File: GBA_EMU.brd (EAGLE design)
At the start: 130.7 x 72.9 mm, 74 parts, among them IC1 MEGA16U2, Q1 MOSFET-PCHANNEL, SW1 LEFT, SW2 RIGHT, SW3 PWR_SWITCH, U1 RPI-ZERO, U2 FT230X, U3 MCP1642B-ADJ, U4 LM4875, U5 V_REG_LDOSMD2, U6 MIC7221, U7 AZV321, X2 HEADPHONE

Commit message: added some descriptions and moved some labels
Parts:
- added R17: 4.7k, rcl:R0805
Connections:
- net N$27 renamed COPRO_TX
- net N$29 renamed COPRO_RX
- net AVR_VCC: now also R17.2
- net RESET: now also R17.1
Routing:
- net RESET: track 36.6 -> 41.0 mm, vias 2 -> 3
- net AVR_VCC: track 65.8 -> 67.3 mm
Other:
- board text added: "GND"
- board text added: "MISO"
- board text added: "MOSI"
- board text added: "RESET"
- board text added: "RX"
- board text added: "SCK"
- board text added: "TX"
- board text added: "VCC"
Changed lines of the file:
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@@
 Taylor Lewis
 Carson Bunker</text>
+<text x="23.876" y="57.404" size="0.6096" layer="21">TX</text>
+<text x="23.876" y="56.134" size="0.6096" layer="21">RX</text>
+<text x="23.368" y="58.674" size="0.6096" layer="21">VCC</text>
+<text x="27.178" y="60.071" size="0.6096" layer="21">GND</text>
+<text x="33.528" y="28.829" size="0.6096" layer="21">MOSI</text>
+<text x="25.654" y="25.146" size="0.6096" layer="21">RESET</text>
+<text x="26.162" y="30.099" size="0.6096" layer="21">SCK</text>
+<text x="25.781" y="31.496" size="0.6096" layer="21">MISO</text>
+<text x="33.401" y="31.242" size="0.6096" layer="21">VCC</text>
 </plain>
 <attributes>
@@
 <attribute name="VALUE" x="98.179" y="84.328" size="1.27" layer="27" rot="R180"/>
 </element>
-<element name="J1" library="SparkFun-Connectors" package="1X04-1.27MM" value="" x="26.035" y="56.515" rot="R90"/>
+<element name="J1" library="SparkFun-Connectors" package="1X04-1.27MM" value="" x="26.035" y="56.515" smashed="yes" rot="R90">
+<attribute name="VALUE" x="27.686" y="56.007" size="0.4064" layer="27" rot="R90"/>
+</element>
+<element name="R17" library="rcl" package="R0805" value="4.7k" x="33.274" y="39.497" smashed="yes" rot="MR180">
+<attribute name="NAME" x="33.909" y="38.227" size="1.0668" layer="26" rot="MR180"/>
+<attribute name="VALUE" x="35.179" y="40.132" size="0.762" layer="28" rot="MR180"/>
+</element>
 </elements>
 <signals>
@@
 <via x="26.035" y="41.275" extent="1-16" drill="0.6"/>
 <wire x1="26.035" y1="41.275" x2="29.21" y2="41.275" width="0.3048" layer="1"/>
-<wire x1="29.21" y1="41.275" x2="29.21" y2="35.56" width="0.3048" layer="1"/>
+<wire x1="29.21" y1="41.275" x2="29.21" y2="37.973" width="0.3048" layer="1"/>
+<wire x1="29.21" y1="37.973" x2="29.21" y2="35.56" width="0.3048" layer="1"/>
 <wire x1="29.21" y1="35.56" x2="31.115" y2="35.56" width="0.3048" layer="1"/>
 <wire x1="31.115" y1="35.56" x2="31.115" y2="34.671" width="0.3048" layer="1"/>
@@
 <wire x1="33.655" y1="27.94" x2="29.21" y2="27.94" width="0.3048" layer="16"/>
 <wire x1="29.21" y1="27.94" x2="29.21" y2="26.67" width="0.3048" layer="16"/>
+<contactref element="R17" pad="1"/>
+<wire x1="32.324" y1="39.497" x2="32.324" y2="38.42" width="0.3048" layer="16"/>
+<wire x1="32.324" y1="38.42" x2="31.877" y2="37.973" width="0.3048" layer="16"/>
+<via x="31.877" y="37.973" extent="1-16" drill="0.6"/>
+<wire x1="31.877" y1="37.973" x2="29.21" y2="37.973" width="0.3048" layer="1"/>
 </signal>
 <signal name="AVR_VCC">
@@
 <via x="30.226" y="59.563" extent="1-16" drill="0.6"/>
 <wire x1="30.226" y1="59.563" x2="31.115" y2="60.325" width="0.3048" layer="16"/>
+<contactref element="R17" pad="2"/>
+<wire x1="34.224" y1="39.497" x2="35.052" y2="39.497" width="0.4064" layer="16"/>
+<wire x1="35.052" y1="39.497" x2="35.56" y2="40.005" width="0.4064" layer="16"/>
 </signal>
 <signal name="COPRO_MOSI">
@@
 <wire x1="94.869" y1="78.359" x2="94.869" y2="73.914" width="0.3048" layer="1"/>
 </signal>
-<signal name="N$27">
+<signal name="COPRO_TX">
 <contactref element="IC1" pad="9"/>
 <contactref element="J1" pad="2"/>
@@
 <wire x1="28.575" y1="57.785" x2="26.035" y2="57.785" width="0.3048" layer="1"/>
 </signal>
-<signal name="N$29">
+<signal name="COPRO_RX">
 <contactref element="IC1" pad="8"/>
 <contactref element="J1" pad="1"/>

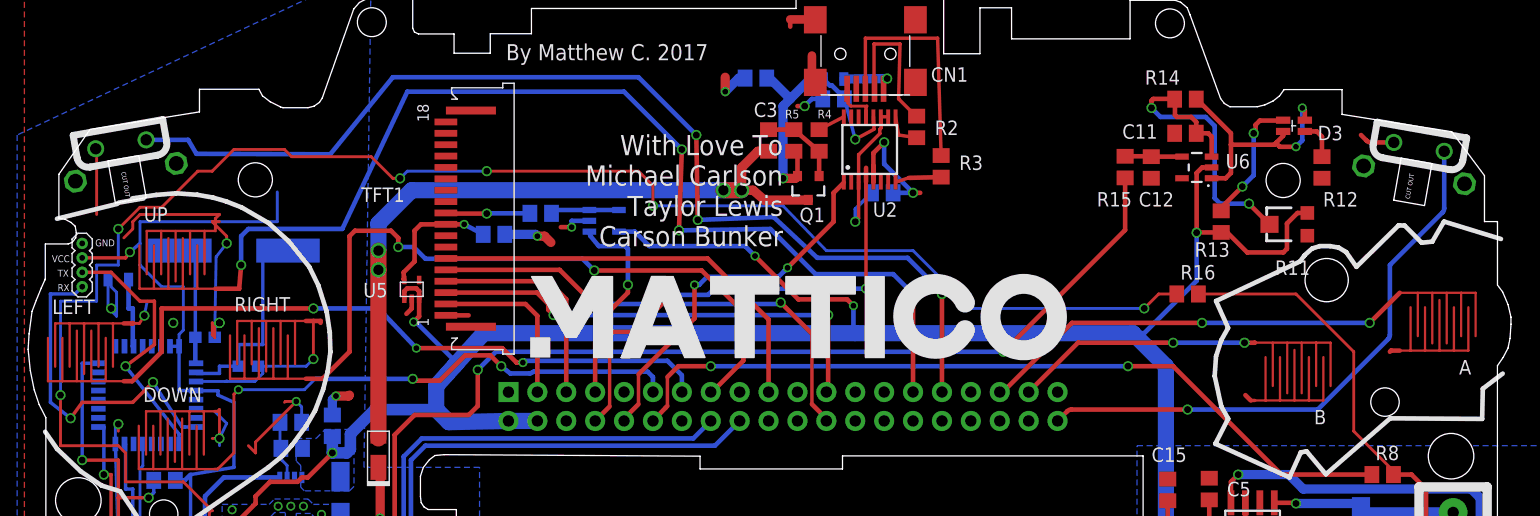
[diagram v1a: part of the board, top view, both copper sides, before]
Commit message: added L2 and R2
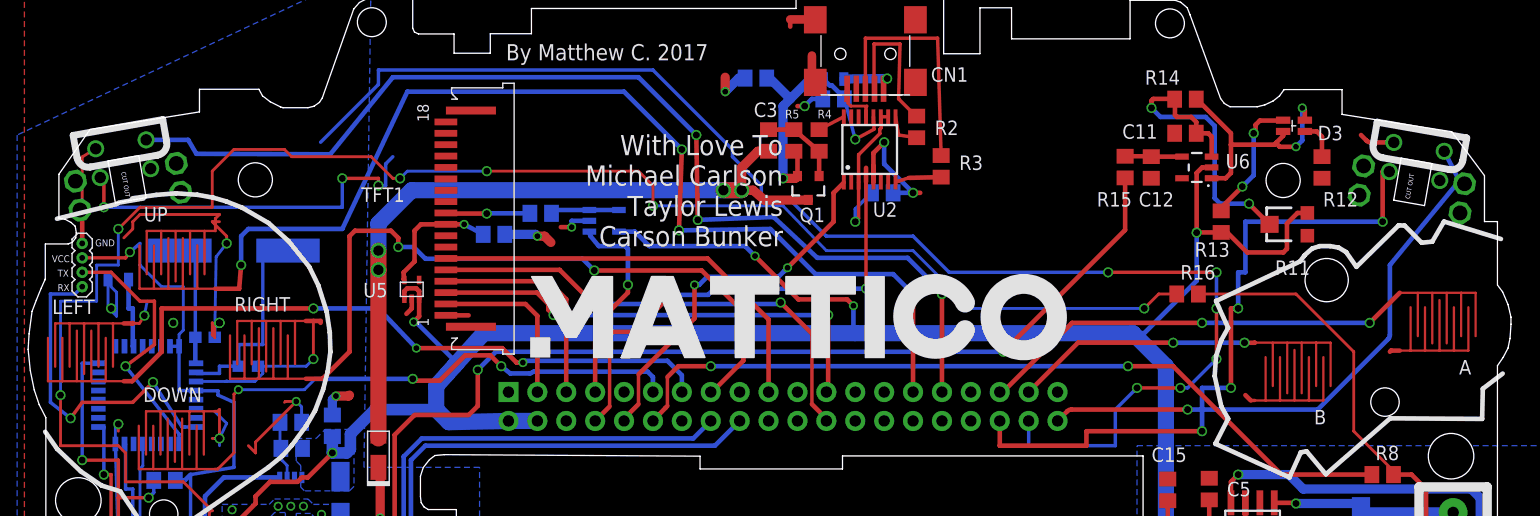
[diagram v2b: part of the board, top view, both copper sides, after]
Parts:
- added SW4: R2, custom:BUMPER_NOHOLE
- added SW5: L2, custom:BUMPER_NOHOLE
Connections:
- removed net DAC_REF: U$5.3
- new net L2_BUMP: SW5.2, U1.38
- new net R2_BUMP: SW4.2, U1.36
- net 3.3V: now also U$5.3
- net GND: now also SW4.1, SW5.1
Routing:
- net L2_BUMP: track 0.00 -> 155.6 mm, vias 0 -> 9
- net R2_BUMP: track 0.00 -> 60.5 mm, vias 0 -> 4
- net AVR_VCC: track 67.3 -> 50.7 mm
- net GND: track 146.2 -> 149.4 mm
- net DAC_OUT: track 160.9 -> 162.8 mm
- net RIGHT_BUMP: track 50.5 -> 51.0 mm
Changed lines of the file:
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@@
 <attribute name="VALUE" x="35.179" y="40.132" size="0.762" layer="28" rot="MR180"/>
 </element>
+<element name="SW4" library="custom" package="BUMPER_NOHOLE" value="R2" x="142.875" y="64.77" rot="MR10"/>
+<element name="SW5" library="custom" package="BUMPER_NOHOLE" value="L2" x="30.099" y="65.024" rot="MR350"/>
 </elements>
 <signals>
@@
 <wire x1="37.737625" y1="62.502625" x2="38.1" y2="62.865" width="0.254" layer="1"/>
 <wire x1="38.1" y1="62.865" x2="31.115" y2="62.865" width="0.254" layer="1"/>
-<wire x1="27.305" y1="62.865" x2="27.305" y2="68.56116875" width="0.254" layer="1"/>
-<wire x1="27.305" y1="68.56116875" x2="27.221940625" y2="68.644228125" width="0.254" layer="1"/>
+<wire x1="26.035" y1="62.23" x2="26.035" y2="67.92616875" width="0.254" layer="1"/>
+<wire x1="26.035" y1="67.92616875" x2="27.221940625" y2="68.644228125" width="0.254" layer="1"/>
 <wire x1="37.677790625" y1="52.067790625" x2="37.68" y2="52.07" width="0.254" layer="1"/>
 <wire x1="28.31" y1="57.15" x2="28.31" y2="54.675859375" width="0.254" layer="16"/>
@@
 <wire x1="88.265" y1="80.01" x2="88.265" y2="79.375" width="0.4064" layer="1"/>
 <wire x1="90.17" y1="74.93" x2="90.17" y2="76.835" width="0.762" layer="1"/>
+<contactref element="SW4" pad="1"/>
+<contactref element="SW5" pad="1"/>
+<wire x1="26.035" y1="62.23" x2="26.035" y2="60.325" width="0.4064" layer="1"/>
 <wire x1="40.64" y1="42.545" x2="38.1" y2="42.545" width="0" layer="19" extent="1-16"/>
+<wire x1="96.52" y1="69.215" x2="94.925" y2="71.455" width="0" layer="19" extent="1-16"/>
 <wire x1="31.75" y1="26.67" x2="39.21125" y2="34.66125" width="0" layer="19" extent="16-16"/>
 </signal>
@@
 <signal name="3.3V">
 <contactref element="U1" pad="1"/>
+<contactref element="U$5" pad="3"/>
+<wire x1="33.95" y1="22.86" x2="63.5" y2="47.26" width="0" layer="19" extent="1-1"/>
 </signal>
 <signal name="2.8V">
@@
 <contactref element="SW2" pad="2"/>
 <contactref element="U1" pad="40"/>
-<wire x1="145.743790625" y1="68.41905" x2="145.743790625" y2="63.4042125" width="0.4064" layer="16"/>
-<wire x1="145.743790625" y1="63.4042125" x2="145.595" y2="63.045" width="0.4064" layer="16" curve="-45.000249"/>
-<wire x1="145.595" y1="63.045" x2="140.97" y2="58.42" width="0.4064" layer="16"/>
+<wire x1="145.743790625" y1="68.41905" x2="147.013790625" y2="65.9442125" width="0.4064" layer="16"/>
+<wire x1="147.013790625" y1="65.9442125" x2="146.865" y2="65.585" width="0.4064" layer="16" curve="-45.000249"/>
+<wire x1="146.865" y1="65.585" x2="140.97" y2="58.42" width="0.4064" layer="16"/>
 <wire x1="140.97" y1="58.42" x2="140.97" y2="52.280421875" width="0.4064" layer="16"/>
 <wire x1="140.97" y1="52.280421875" x2="140.821209375" y2="51.921209375" width="0.4064" layer="16" curve="-45.000249"/>
@@
 <wire x1="43.815" y1="68.58" x2="39.37" y2="68.58" width="0.254" layer="1"/>
 <wire x1="39.37" y1="68.58" x2="37.465" y2="66.675" width="0.254" layer="1"/>
-<wire x1="37.465" y1="66.675" x2="36.195" y2="66.675" width="0.254" layer="1"/>
-<wire x1="36.195" y1="66.675" x2="33.02" y2="63.5" width="0.254" layer="1"/>
-<wire x1="33.02" y1="63.5" x2="31.115" y2="63.5" width="0.254" layer="1"/>
+<wire x1="37.465" y1="66.675" x2="37.465" y2="63.5" width="0.254" layer="1"/>
+<wire x1="37.465" y1="63.5" x2="31.115" y2="63.5" width="0.254" layer="1"/>
 <wire x1="31.115" y1="63.5" x2="29.21" y2="61.595" width="0.254" layer="1"/>
 <via x="29.21" y="61.595" extent="1-16" drill="0.6"/>
@@
 <wire x1="33.02" y1="56.515" x2="31.115" y2="58.42" width="0.254" layer="16"/>
 <wire x1="31.115" y1="58.42" x2="31.115" y2="60.325" width="0.254" layer="16"/>
-<wire x1="31.115" y1="60.325" x2="31.115" y2="62.23" width="0.254" layer="16"/>
-<wire x1="31.115" y1="62.23" x2="43.18" y2="62.23" width="0.254" layer="16"/>
-<wire x1="43.18" y1="62.23" x2="43.18" y2="64.85" width="0.254" layer="16"/>
 <contactref element="J1" pad="3"/>
 <wire x1="26.035" y1="59.055" x2="29.845" y2="59.055" width="0.3048" layer="1"/>
@@
 <wire x1="31.369" y1="42.6784" x2="31.35" y2="42.6974" width="0.254" layer="16"/>
 </signal>
-<signal name="DAC_REF">
-<contactref element="U$5" pad="3"/>
-</signal>
 <signal name="N$4">
 <contactref element="R2" pad="2"/>
@@
 <wire x1="25.4" y1="55.88" x2="26.035" y2="56.515" width="0.3048" layer="16"/>
 </signal>
+<signal name="R2_BUMP">
+<contactref element="SW4" pad="2"/>
+<contactref element="U1" pad="36"/>
+<wire x1="140.91965625" y1="66.63791875" x2="140.335" y2="66.63791875" width="0.4064" layer="1"/>
+<wire x1="140.335" y1="66.63791875" x2="140.335" y2="62.23" width="0.4064" layer="1"/>
+<via x="140.335" y="62.23" extent="1-16" drill="0.6"/>
+<wire x1="140.335" y1="62.23" x2="128.27" y2="62.23" width="0.4064" layer="16"/>
+<wire x1="128.27" y1="62.23" x2="128.27" y2="57.785" width="0.4064" layer="16"/>
+<wire x1="128.27" y1="57.785" x2="127.635" y2="57.785" width="0.4064" layer="16"/>
+<wire x1="127.635" y1="57.785" x2="127.635" y2="54.61" width="0.4064" layer="16"/>
+<via x="127.635" y="54.61" extent="1-16" drill="0.6"/>
+<wire x1="127.635" y1="54.61" x2="127" y2="54.61" width="0.4064" layer="1"/>
+<wire x1="127" y1="54.61" x2="127" y2="47.625" width="0.4064" layer="1"/>
+<via x="127" y="47.625" extent="1-16" drill="0.6"/>
+<wire x1="127" y1="47.625" x2="124.46" y2="47.625" width="0.4064" layer="16"/>
+<wire x1="124.46" y1="47.625" x2="124.46" y2="43.815" width="0.4064" layer="16"/>
+<via x="124.46" y="43.815" extent="1-16" drill="0.6"/>
+<wire x1="124.46" y1="43.815" x2="114.3" y2="43.815" width="0.4064" layer="1"/>
+<wire x1="114.3" y1="43.815" x2="114.3" y2="42.545" width="0.4064" layer="1"/>
+<wire x1="114.3" y1="42.545" x2="106.68" y2="42.545" width="0.4064" layer="1"/>
+<wire x1="106.68" y1="42.545" x2="106.68" y2="44.72" width="0.4064" layer="1"/>
+</signal>
+<signal name="L2_BUMP">
+<contactref element="SW5" pad="2"/>
+<contactref element="U1" pad="38"/>
+<wire x1="27.6227125" y1="66.110503125" x2="27.94" y2="66.110503125" width="0.3048" layer="1"/>
+<wire x1="27.94" y1="66.110503125" x2="27.94" y2="63.5" width="0.3048" layer="1"/>
+<via x="27.94" y="63.5" extent="1-16" drill="0.6" shape="square"/>
+<wire x1="27.94" y1="63.5" x2="48.895" y2="63.5" width="0.3048" layer="16"/>
+<wire x1="48.895" y1="63.5" x2="48.895" y2="66.04" width="0.3048" layer="16"/>
+<via x="48.895" y="66.04" extent="1-16" drill="0.6" shape="square"/>
+<wire x1="48.895" y1="66.04" x2="52.07" y2="66.04" width="0.3048" layer="1"/>
+<wire x1="52.07" y1="66.04" x2="52.07" y2="65.405" width="0.3048" layer="1"/>
+<via x="52.07" y="65.405" extent="1-16" drill="0.6" shape="square"/>
+<wire x1="52.07" y1="65.405" x2="52.705" y2="65.405" width="0.3048" layer="16"/>
+<wire x1="52.705" y1="65.405" x2="52.705" y2="67.31" width="0.3048" layer="16"/>
+<wire x1="52.705" y1="67.31" x2="53.34" y2="67.945" width="0.3048" layer="16"/>
+<wire x1="109.22" y1="44.72" x2="109.22" y2="42.545" width="0.3048" layer="16"/>
+<wire x1="109.22" y1="42.545" x2="116.84" y2="42.545" width="0.3048" layer="16"/>
+<wire x1="116.84" y1="42.545" x2="116.84" y2="45.72" width="0.3048" layer="16"/>
+<wire x1="116.84" y1="45.72" x2="118.745" y2="47.625" width="0.3048" layer="16"/>
+<via x="118.745" y="47.625" extent="1-16" drill="0.6" shape="square"/>
+<wire x1="118.745" y1="47.625" x2="122.555" y2="47.625" width="0.3048" layer="1"/>
+<via x="122.555" y="47.625" extent="1-16" drill="0.6" shape="square"/>
+<wire x1="122.555" y1="47.625" x2="123.19" y2="47.625" width="0.3048" layer="16"/>
+<wire x1="123.19" y1="47.625" x2="125.73" y2="50.165" width="0.3048" layer="16"/>
+<via x="125.73" y="50.165" extent="1-16" drill="0.6" shape="square"/>
+<wire x1="125.73" y1="50.165" x2="125.73" y2="54.61" width="0.3048" layer="1"/>
+<via x="125.73" y="54.61" extent="1-16" drill="0.6" shape="square"/>
+<wire x1="125.73" y1="54.61" x2="125.73" y2="57.785" width="0.3048" layer="16"/>
+<via x="125.73" y="57.785" extent="1-16" drill="0.6" shape="square"/>
+<wire x1="125.73" y1="57.785" x2="116.205" y2="57.785" width="0.3048" layer="1"/>
+<via x="116.205" y="57.785" extent="1-16" drill="0.6" shape="square"/>
+<wire x1="116.205" y1="57.785" x2="102.235" y2="57.785" width="0.3048" layer="16"/>
+<wire x1="102.235" y1="57.785" x2="99.06" y2="60.96" width="0.3048" layer="16"/>
+<wire x1="99.06" y1="60.96" x2="91.44" y2="60.96" width="0.3048" layer="16"/>
+<wire x1="91.44" y1="60.96" x2="88.265" y2="64.135" width="0.3048" layer="16"/>
+<wire x1="88.265" y1="64.135" x2="85.725" y2="64.135" width="0.3048" layer="16"/>
+<wire x1="85.725" y1="64.135" x2="85.725" y2="65.405" width="0.3048" layer="16"/>
+<wire x1="85.725" y1="65.405" x2="83.185" y2="67.945" width="0.3048" layer="16"/>
+<wire x1="83.185" y1="67.945" x2="83.185" y2="68.58" width="0.3048" layer="16"/>
+<wire x1="83.185" y1="68.58" x2="76.2" y2="75.565" width="0.3048" layer="16"/>
+<wire x1="76.2" y1="75.565" x2="52.07" y2="75.565" width="0.3048" layer="16"/>
+<wire x1="52.07" y1="75.565" x2="52.07" y2="74.295" width="0.3048" layer="16"/>
+<wire x1="52.07" y1="74.295" x2="46.99" y2="69.215" width="0.3048" layer="16"/>
+<wire x1="46.99" y1="69.215" x2="48.895" y2="66.04" width="0" layer="19" extent="1-16"/>
+</signal>
 </signals>

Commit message: almost done!
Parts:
- removed X2: HEADPHONE, GBA:HEADPHONE
- added J2: AUDIO-JACK2SMD, SparkFun-Connectors:AUDIO-JACK-3.5MM-SMD
- added POT1: THUMBPOT, adafruit:THUMBWHEEL
- R1: value 27k -> 150R; device GBA:VOLUME -> SparkFun-Resistors:0603-RES
- moved R1 10.4 mm to (127.6, 23.5), flipped to the top, turned to 270 degrees
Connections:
- removed net N$13: C7.-, X2.L, X2.R
- new net N$29: C7.-, J2.RING, J2.TIP, R1.2
- net 5V: now also POT1.3; no longer R1.5
- net GND: now also J2.SLEEVE, POT1.1; no longer X2.1, X2.GND
- net N$16: now also J2.TSH; no longer X2.2
- net N$8: now also POT1.2; no longer R1.3
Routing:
- net N$29: track 0.00 -> 45.7 mm, vias 0 -> 3
- net N$13: track 34.5 -> 0.00 mm, vias 1 -> 0
- net GND: track 149.4 -> 178.2 mm
- net 5V: track 232.9 -> 248.3 mm
- net N$16: track 16.6 -> 23.1 mm
- net N$8: track 8.86 -> 11.1 mm, vias 1 -> 0
